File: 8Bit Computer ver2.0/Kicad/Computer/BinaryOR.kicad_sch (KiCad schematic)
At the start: 4 parts, among them IC23 SN74LVC1G14DBVR, IC26 SN74HCS74DR, IC27 SN74ABT821ADWR, IC28 SN74HCS32DR

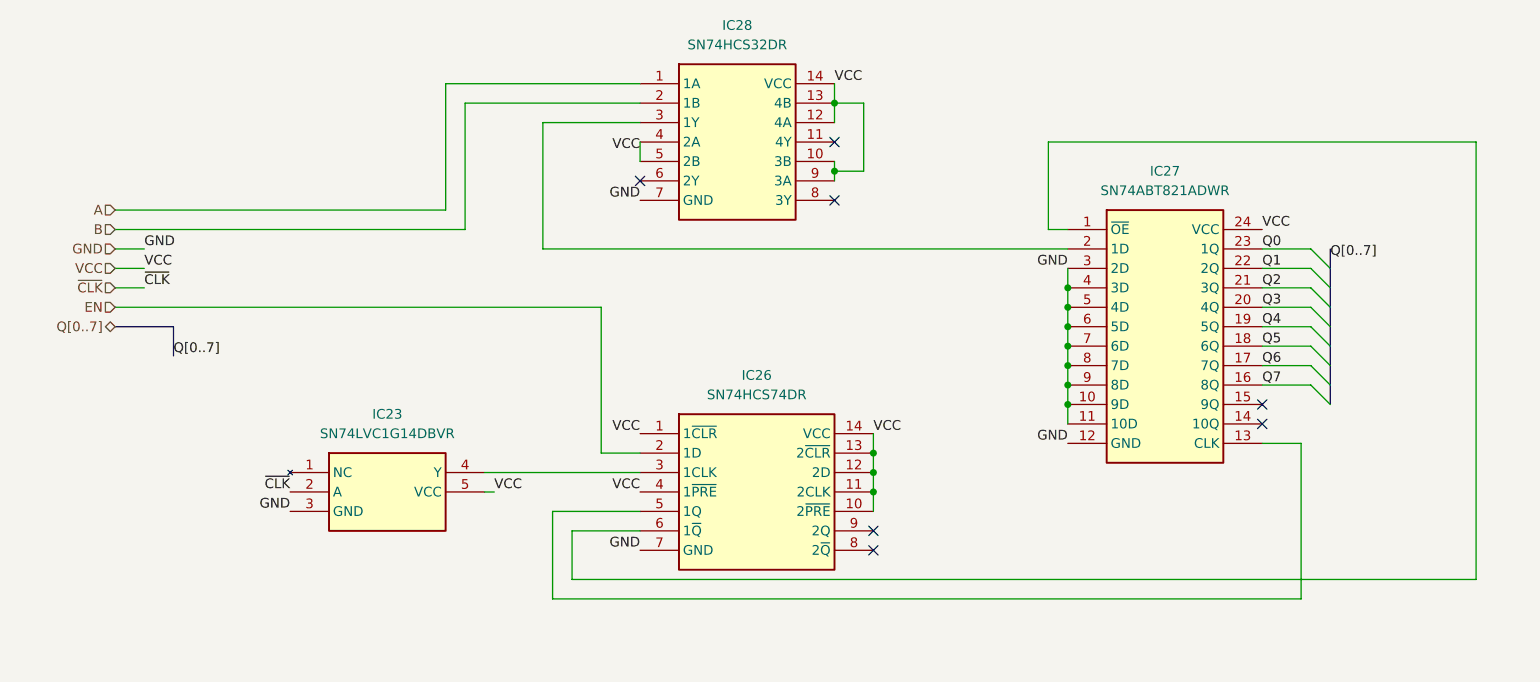
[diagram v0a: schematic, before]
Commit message: parts,Kicad
parts:
changed 8xDlatch HCS to ABT 574
waiting for SRAM CAD Model
Kicad:
imported AHC types of ICs
added ProgrammeCounter
finished Comparator
changed all HCS to AHC except 3in OR ->no AHC Version
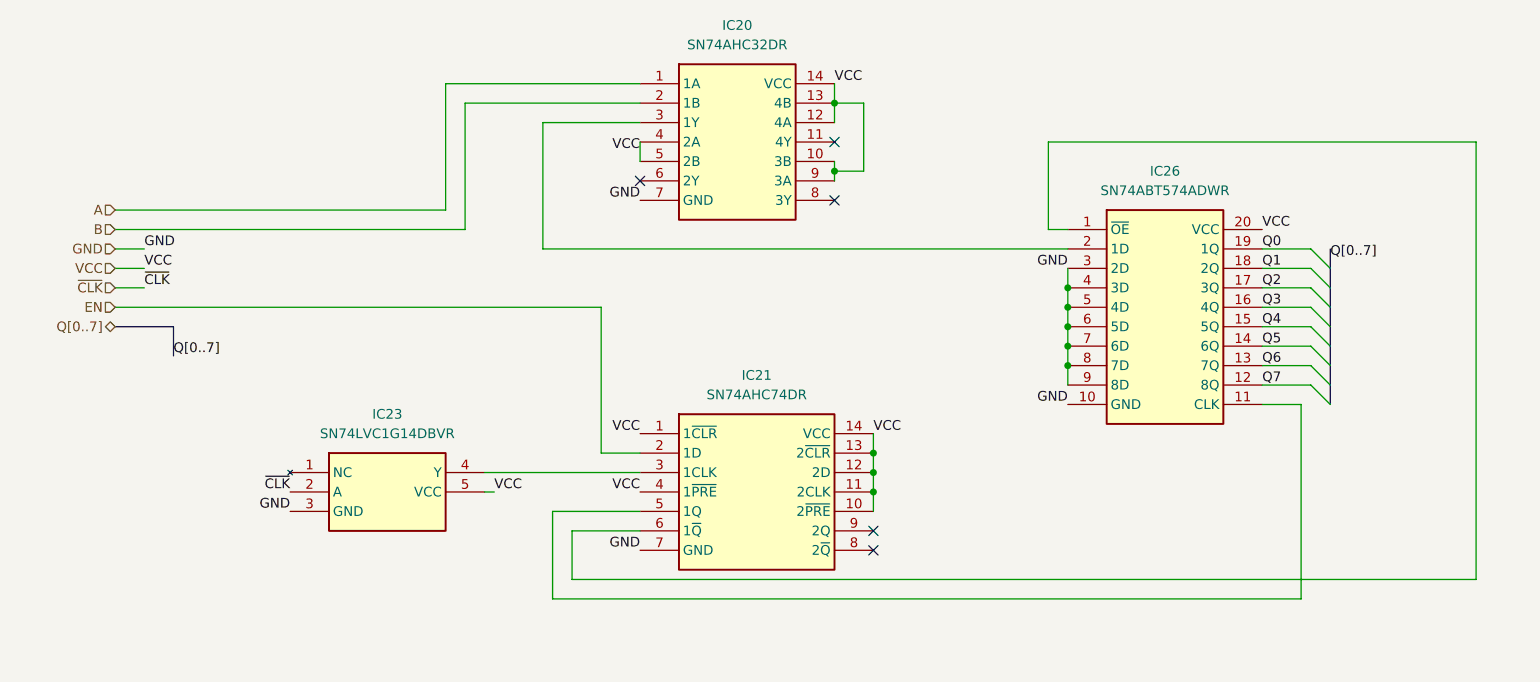
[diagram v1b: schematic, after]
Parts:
- removed IC26: SN74HCS74DR, Samacsys:SOIC127P600X175-14N, symbol Samacsys:SN74HCS74DR
- removed IC27: SN74ABT821ADWR, Samacsys:SOIC127P1030X265-24N, symbol Samacsys:SN74ABT821ADWR
- removed IC28: SN74HCS32DR, Samacsys:SOIC127P600X175-14N, symbol Samacsys:SN74HCS32DR
- added IC20: SN74AHC32DR, Samacsys:SOIC127P600X175-14N, symbol Samacsys:SN74AHC32DR
- added IC21: SN74AHC74DR, Samacsys:SOIC127P600X175-14N, symbol Samacsys:SN74AHC74DR
- added IC26: SN74ABT574ADWR, Samacsys:SOIC127P1030X265-20N, symbol Samacsys:SN74ABT574ADWR
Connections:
- net A: now also IC20.1 (1A)
- net B: now also IC20.2 (1B)
- net EN: now also IC21.2 (1D)
- net GND: now also IC20.7 (GND), IC21.7 (GND), IC26.10 (GND), IC26.3 (2D), IC26.4 (3D), IC26.5 (4D), IC26.6 (5D), IC26.7 (6D), IC26.8 (7D), IC26.9 (8D)
- net Q0: now also IC26.19 (1Q)
- net Q1: now also IC26.18 (2Q)
- net Q2: now also IC26.17 (3Q)
- net Q3: now also IC26.16 (4Q)
- net Q4: now also IC26.15 (5Q)
- net Q5: now also IC26.14 (6Q)
- net Q6: now also IC26.13 (7Q)
- net Q7: now also IC26.12 (8Q)
- net VCC: now also IC20.10 (3B), IC20.12 (4A), IC20.13 (4B), IC20.14 (VCC), IC20.4 (2A), IC20.5 (2B), IC20.9 (3A), IC21.1 (1~{CLR}), IC21.10 (2~{PRE}), IC21.11 (2CLK), IC21.12 (2D), IC21.13 (2~{CLR}), IC21.14 (VCC), IC21.4 (1~{PRE}), IC26.20 (VCC)
- net at IC23.4 (Y): now also IC21.3 (1CLK)
- new net: IC20.3 (1Y), IC26.2 (1D)
- new net: IC21.5 (1Q), IC26.11 (CLK)
- new net: IC21.6 (1~{Q}), IC26.1 (~{OE})
- no-connect marks 7 -> 5

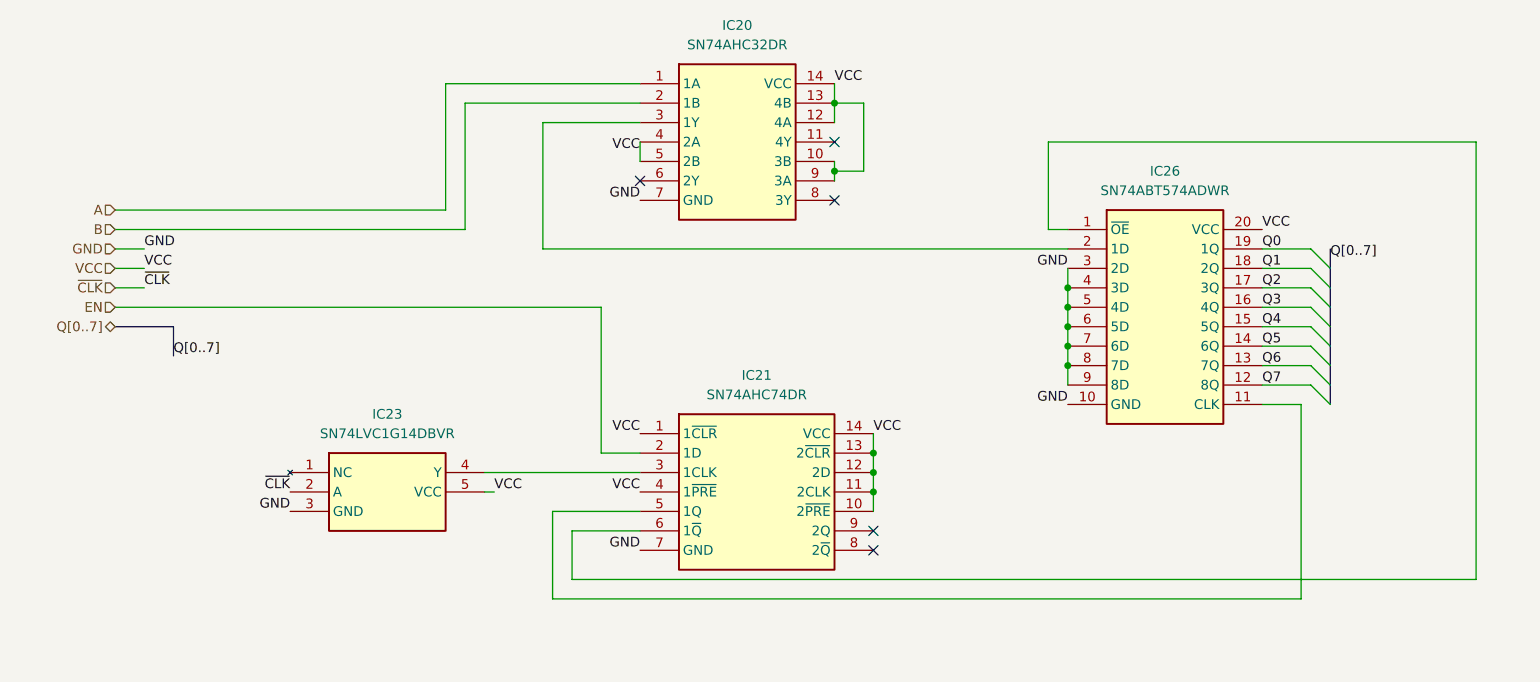
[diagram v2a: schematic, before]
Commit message: Kicad, parts
Parts:
added Leds
Kicad:
added Input Output
changed Q bus to DAT bus
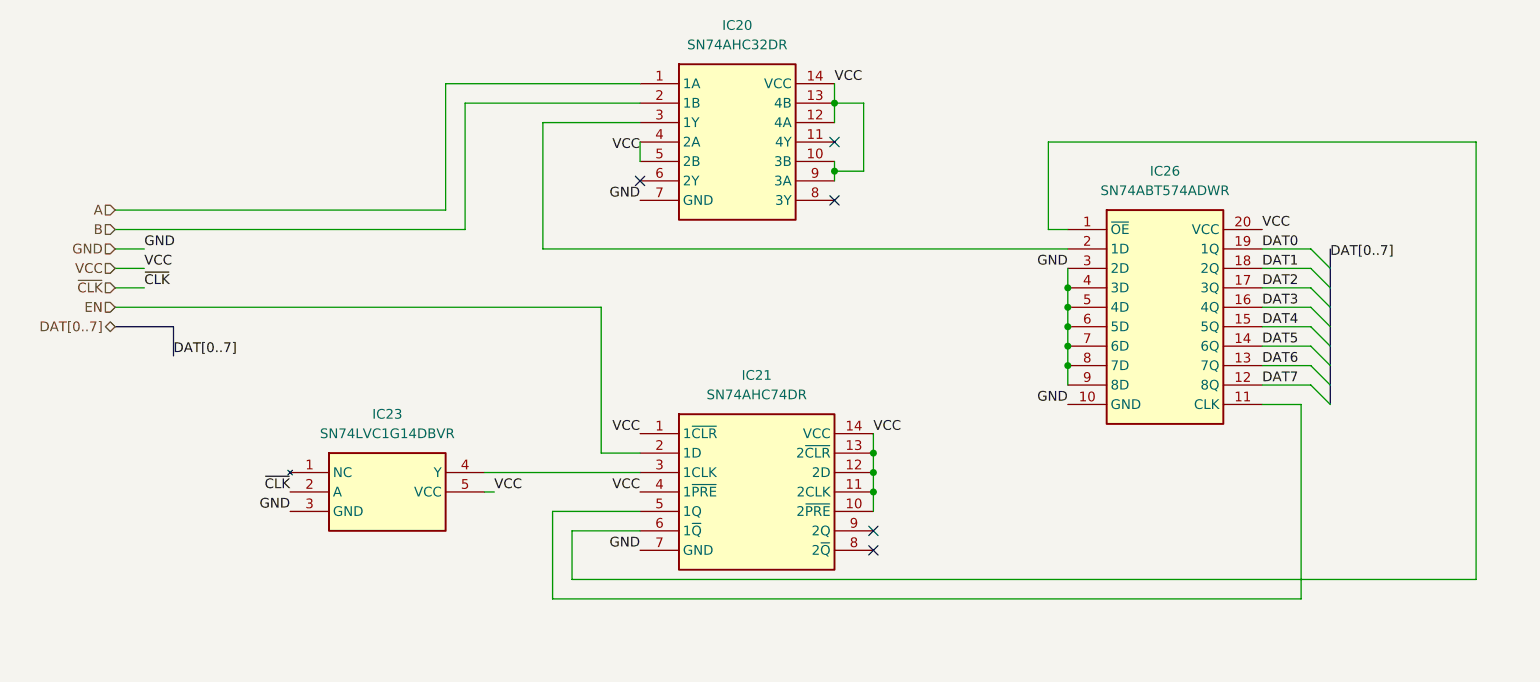
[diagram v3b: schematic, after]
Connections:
- net Q0 renamed DAT0
- net Q1 renamed DAT1
- net Q2 renamed DAT2
- net Q3 renamed DAT3
- net Q4 renamed DAT4
- net Q5 renamed DAT5
- net Q6 renamed DAT6
- net Q7 renamed DAT7
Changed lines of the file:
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@@
 		)
 	)
-	(label "Q1"
+	(label "DAT1"
 		(at 205.74 82.55 0)
 		(effects
@@
 		)
 	)
-	(label "Q4"
+	(label "DAT4"
 		(at 205.74 90.17 0)
 		(effects
@@
 		)
 	)
-	(label "Q3"
+	(label "DAT3"
 		(at 205.74 87.63 0)
 		(effects
@@
 		)
 	)
-	(label "Q0"
+	(label "DAT0"
 		(at 205.74 80.01 0)
 		(effects
@@
 		)
 	)
-	(label "Q5"
+	(label "DAT5"
 		(at 205.74 92.71 0)
 		(effects
@@
 		)
 	)
-	(label "Q[0..7]"
+	(label "DAT[0..7]"
 		(at 214.63 81.28 0)
 		(effects
@@
 		)
 	)
-	(label "Q2"
+	(label "DAT2"
 		(at 205.74 85.09 0)
 		(effects
@@
 		)
 	)
-	(label "Q7"
+	(label "DAT7"
 		(at 205.74 97.79 0)
 		(effects
@@
 		)
 	)
-	(label "Q[0..7]"
+	(label "DAT[0..7]"
 		(at 63.5 93.98 0)
 		(effects
@@
 		)
 	)
-	(label "Q6"
+	(label "DAT6"
 		(at 205.74 95.25 0)
 		(effects
@@
 		)
 	)
-	(hierarchical_label "Q[0..7]"
+	(hierarchical_label "DAT[0..7]"
 		(shape tri_state)
 		(at 55.88 90.17 180)

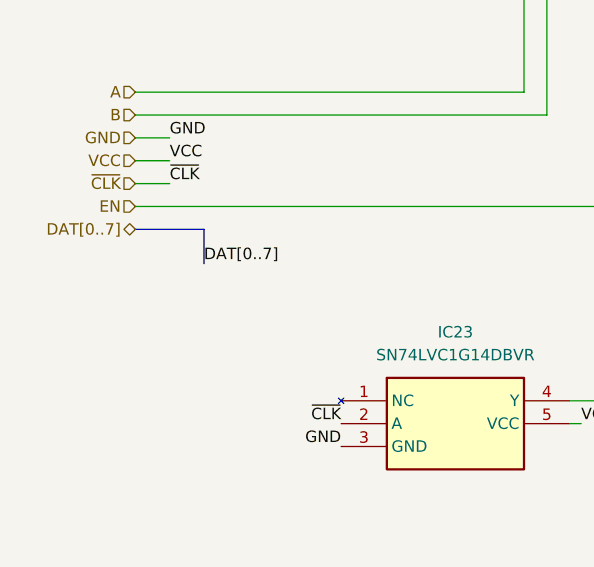
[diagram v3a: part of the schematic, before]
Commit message: Kicad, parts
parts:
added USB C PD Triggerboard
added Delay Chip for 90ns
added Push Button
Kicad:
added USB C PD Triggerboard
added rising edge detector via Delay and Xor for Accept Push Button
added VBUS net
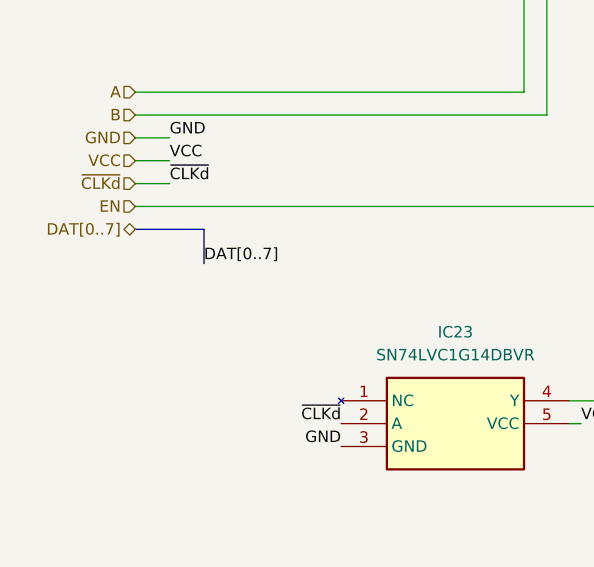
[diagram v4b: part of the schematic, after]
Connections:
- net ~{CLK} renamed ~{CLKd}
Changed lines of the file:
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@@
 		)
 	)
-	(label "~{CLK}"
+	(label "~{CLKd}"
 		(at 59.69 85.09 0)
 		(effects
@@
 		)
 	)
-	(label "~{CLK}"
+	(label "~{CLKd}"
 		(at 78.74 111.76 180)
 		(effects
@@
 		)
 	)
-	(hierarchical_label "~{CLK}"
+	(hierarchical_label "~{CLKd}"
 		(shape input)
 		(at 55.88 85.09 180)

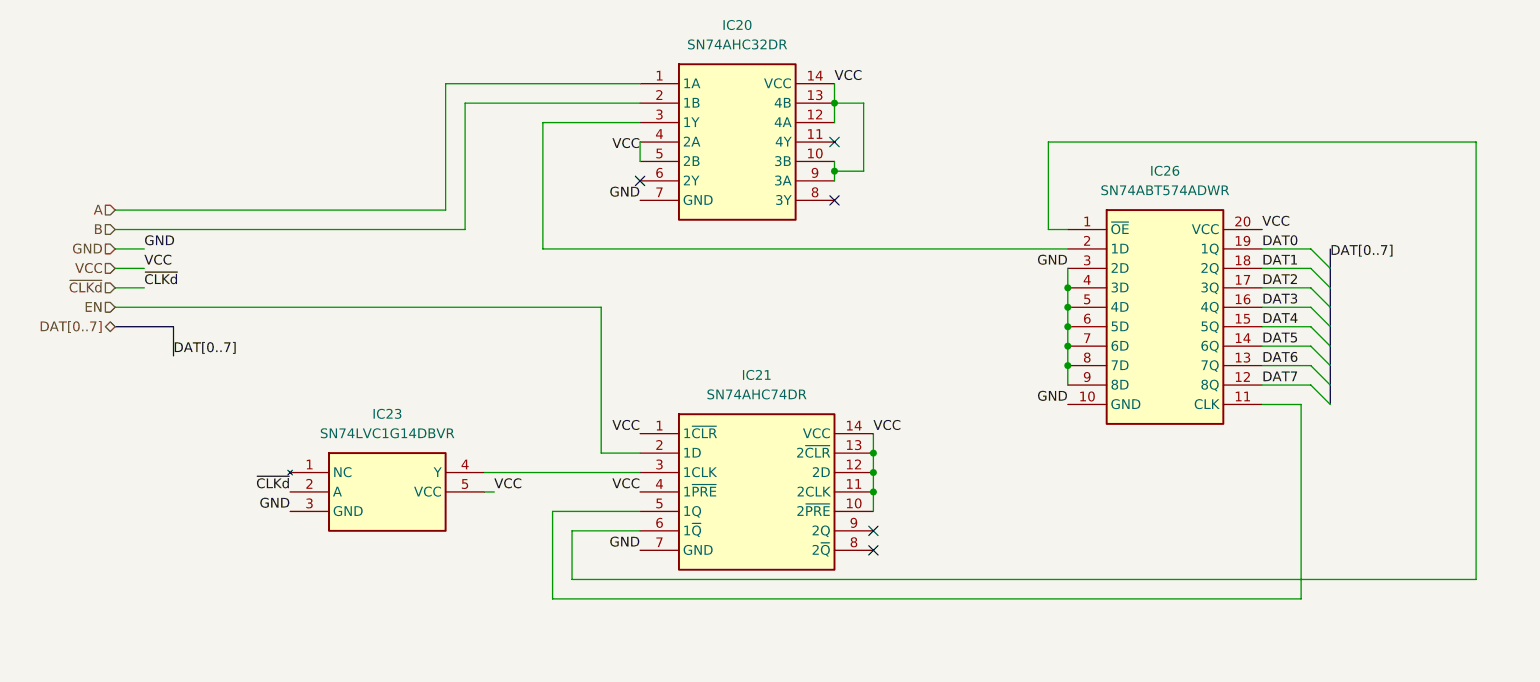
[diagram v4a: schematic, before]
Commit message: Kicad SCH/PCB
Kicad SCH/PCB:
changed the References in SCH
began with INOUTPUT module nearly done
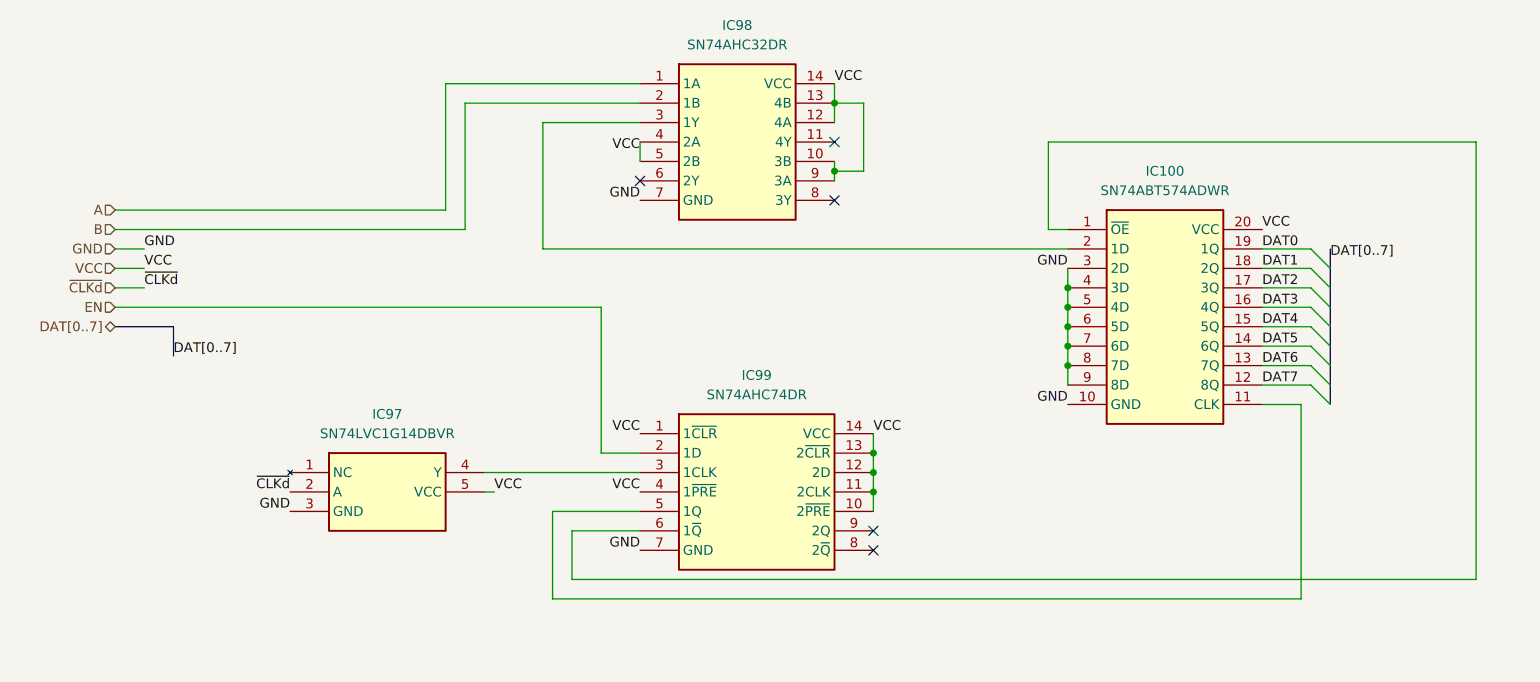
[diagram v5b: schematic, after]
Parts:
- renumbered IC26 to IC100, IC23 to IC97, IC20 to IC98, IC21 to IC99
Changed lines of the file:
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@@
 		(dnp no)
 		(fields_autoplaced yes)
-		(property "Reference" "IC23"
+		(property "Reference" "IC97"
 			(at 91.44 101.6 0)
 			(effects
@@
 			(project "Computer"
 				(path "/1196a00e-6878-4d6d-82b7-9e052dfe7c14/c4d8b530-1c6d-45af-88d2-7dc1d4321a34/f378dbdf-df8b-4230-93b7-3ecbbffd1ccb"
-					(reference "IC23")
+					(reference "IC97")
 					(unit 1)
 				)
@@
 		(dnp no)
 		(fields_autoplaced yes)
-		(property "Reference" "IC20"
+		(property "Reference" "IC98"
 			(at 137.16 50.8 0)
 			(effects
@@
 			(project "Computer"
 				(path "/1196a00e-6878-4d6d-82b7-9e052dfe7c14/c4d8b530-1c6d-45af-88d2-7dc1d4321a34/f378dbdf-df8b-4230-93b7-3ecbbffd1ccb"
-					(reference "IC20")
+					(reference "IC98")
 					(unit 1)
 				)
@@
 		(dnp no)
 		(fields_autoplaced yes)
-		(property "Reference" "IC21"
+		(property "Reference" "IC99"
 			(at 139.7 96.52 0)
 			(effects
@@
 			(project "Computer"
 				(path "/1196a00e-6878-4d6d-82b7-9e052dfe7c14/c4d8b530-1c6d-45af-88d2-7dc1d4321a34/f378dbdf-df8b-4230-93b7-3ecbbffd1ccb"
-					(reference "IC21")
+					(reference "IC99")
 					(unit 1)
 				)
@@
 		(dnp no)
 		(fields_autoplaced yes)
-		(property "Reference" "IC26"
+		(property "Reference" "IC100"
 			(at 193.04 69.85 0)
 			(effects
@@
 			(project "Computer"
 				(path "/1196a00e-6878-4d6d-82b7-9e052dfe7c14/c4d8b530-1c6d-45af-88d2-7dc1d4321a34/f378dbdf-df8b-4230-93b7-3ecbbffd1ccb"
-					(reference "IC26")
+					(reference "IC100")
 					(unit 1)
 				)
